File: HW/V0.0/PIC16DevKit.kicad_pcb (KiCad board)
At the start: 4 copper layers, 68.8 x 54 mm, 115 parts, among them J1 9V-12V, J2 USB C, J3 EXP PORT, J4 PG ICSP, Q1 SI2301, Q2 SI2302, Q3 SI2301, Q4 2N3906, Q5 SI2302, Q6 SI2302, Q7 SI2302, U1 LDO 3.3V/300mA, U10 20MHz, U11 PIC32MM0064GPM028, U2 MT1470, U3 MT3608, U4 PIC16F877A, U6 SN74LVC1T45, U7 SN74LVC1T45, U8 SN74LVC1T45, U9 SN74LVC1T45

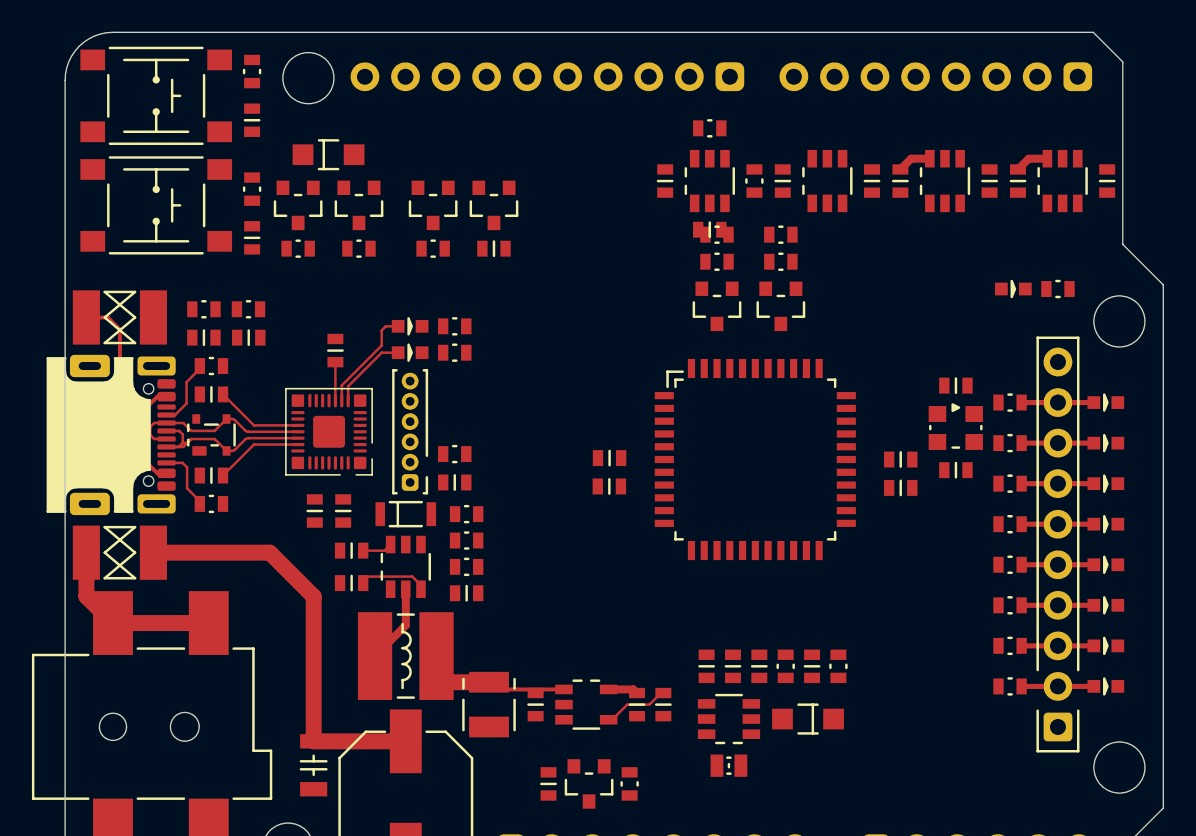
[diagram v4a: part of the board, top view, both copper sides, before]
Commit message: PIC16-DevKit-PCB-877 layout update 2
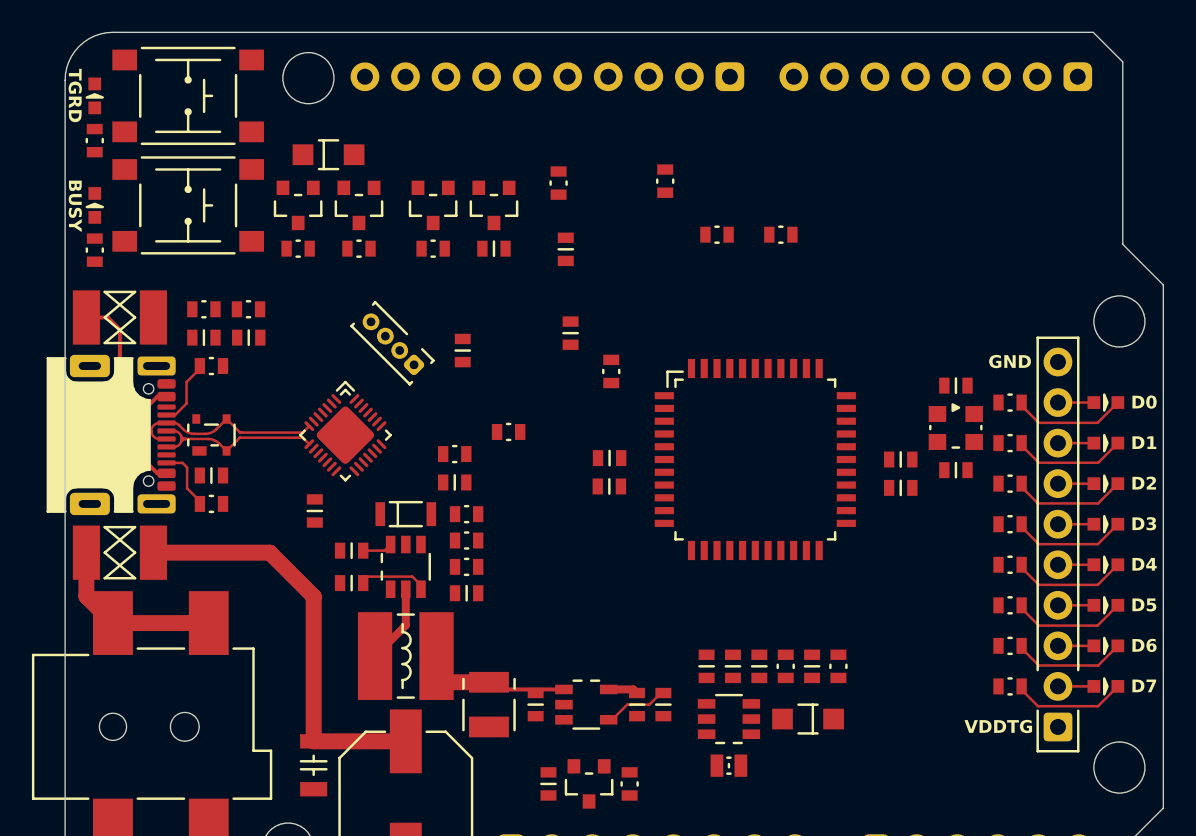
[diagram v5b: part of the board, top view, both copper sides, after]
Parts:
- removed C23, C24, C28, C30, C31, C33, C34, C35, C36: 100nF, SAMPI:CAP0603
- removed C29: 10uF, SAMPI:CAP0603
- removed D5: ULED, SAMPI:LED0603
- removed Q6, Q7: SI2302, SAMPI:SOT23
- removed R28, R30, R31: 5.1K, 1%, SAMPI:RES0603
- removed U11: PIC32MM0064GPM028, SAMPI:UQFN28-4x4-EP
- removed U6, U7, U8, U9: SN74LVC1T45, SAMPI:SOT-23-6_MCHP
- added U5: AVRxxDU28, SAMPI:VQFN28-4x4-EP, F.Cu at (78.2, 68.3)
- D10: value RD5 -> D2
- D11: value RD4 -> D3
- D12: value RD3 -> D4
- D13: value RD2 -> D5
- D14: value RD1 -> D6
- D15: value RD0 -> D7
- D6: value TARGET -> TGRD
- D8: value RD7 -> D0
- D9: value RD6 -> D1
- J4: value PG ICSP -> SIL04; footprint SAMPI:HD-1x6x1.27MM-TH -> SAMPI:HD-1x4x1.27MM-TH
- R19: value 330R -> 5.1K, 1%
- moved R19 35.6 mm to (88.5, 68.1)
- moved R24 26.2 mm to (62.5, 49.8), turned to 90 degrees
- moved D6 25.5 mm to (62.5, 47.0), turned to -90 degrees
- moved R23 25.2 mm to (94.9, 64.3)
- moved R25 23.0 mm to (62.5, 56.7), turned to 90 degrees
- moved C17 21.2 mm to (92.0, 56.6)
- moved D7 21.2 mm to (62.5, 53.9), turned to -90 degrees
- moved C22 20.8 mm to (92.3, 61.9)
- moved R18 20.4 mm to (91.6, 52.5)
- moved C25 7.98 mm to (85.6, 63.0)
- moved J4 5.65 mm to (81.2, 62.5), turned to 135 degrees
- moved R27 4.33 mm to (98.3, 52.4), turned to -90 degrees
- moved BT1 2.00 mm to (68.4, 53.9)
- moved BT2 2.00 mm to (68.4, 47.0)
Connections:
- net /PROGRAMMER/CS renamed /PROGRAMMER/TG_MCLR
- net /PROGRAMMER/~{PG_MCLR} renamed /PROGRAMMER/~{PG_RESET}
- C25 pad 1: +3.3V -> +5V
- C26 pad 1: +3.3V -> +5V
- C27 pad 1: +3.3V -> +5V
- D10 pad A: Net-(D10-PadA) -> /TARGET MCU/RD2
- D10 pad K: GND -> Net-(D10-PadK)
- D11 pad A: Net-(D11-PadA) -> /TARGET MCU/RD3
- D11 pad K: GND -> Net-(D11-PadK)
- D12 pad A: Net-(D12-PadA) -> /TARGET MCU/RD4
- D12 pad K: GND -> Net-(D12-PadK)
- D13 pad A: Net-(D13-PadA) -> /TARGET MCU/RD5
- D13 pad K: GND -> Net-(D13-PadK)
- D14 pad A: Net-(D14-PadA) -> /TARGET MCU/RD6
- D14 pad K: GND -> Net-(D14-PadK)
- D15 pad A: Net-(D15-PadA) -> /TARGET MCU/RD7
- D15 pad K: GND -> Net-(D15-PadK)
- D6 pad A: /PROGRAMMER/LED_TGRDY -> Net-(D6-PadA)
- D6 pad K: Net-(D6-PadK) -> GND
- D7 pad A: /PROGRAMMER/LED_BUSY -> Net-(D7-PadA)
- D7 pad K: Net-(D7-PadK) -> GND
- D8 pad A: Net-(D8-PadA) -> /TARGET MCU/RD0
- D8 pad K: GND -> Net-(D8-PadK)
- D9 pad A: Net-(D9-PadA) -> /TARGET MCU/RD1
- D9 pad K: GND -> Net-(D9-PadK)
- J3 pad 2: Net-(D15-PadA) -> /TARGET MCU/RD7
- J3 pad 3: Net-(D14-PadA) -> /TARGET MCU/RD6
- J3 pad 4: Net-(D13-PadA) -> /TARGET MCU/RD5
- J3 pad 5: Net-(D12-PadA) -> /TARGET MCU/RD4
- J3 pad 6: Net-(D11-PadA) -> /TARGET MCU/RD3
- J3 pad 7: Net-(D10-PadA) -> /TARGET MCU/RD2
- J3 pad 8: Net-(D9-PadA) -> /TARGET MCU/RD1
- J3 pad 9: Net-(D8-PadA) -> /TARGET MCU/RD0
- J4 pad 2: +3.3V -> +5V
- J4 pad 4: /PROGRAMMER/PG_PGD -> /PROGRAMMER/PG_UPDI
- MD1 pad 15: /PROGRAMMER/~{TG_RXD} -> /PROGRAMMER/TXD1
- MD1 pad 16: /PROGRAMMER/~{TG_TXD} -> /PROGRAMMER/RXD1
- MD1 pad 19: /TARGET MCU/ULED -> /TARGET MCU/GPIO
- MD1 pad 31: /PROGRAMMER/TG_SDA -> /PROGRAMMER/SDA
- MD1 pad 32: /PROGRAMMER/TG_SCL -> /PROGRAMMER/SCL
- R11 pad 1: /TARGET MCU/RD0 -> GND
- R11 pad 2: Net-(D15-PadA) -> Net-(D15-PadK)
- R12 pad 1: /TARGET MCU/RD1 -> GND
- R12 pad 2: Net-(D14-PadA) -> Net-(D14-PadK)
- R13 pad 1: /TARGET MCU/RD2 -> GND
- R13 pad 2: Net-(D13-PadA) -> Net-(D13-PadK)
- R14 pad 1: /TARGET MCU/RD3 -> GND
- R14 pad 2: Net-(D12-PadA) -> Net-(D12-PadK)
- R15 pad 1: /TARGET MCU/RD4 -> GND
- R15 pad 2: Net-(D11-PadA) -> Net-(D11-PadK)
- R16 pad 1: /TARGET MCU/RD5 -> GND
- R16 pad 2: Net-(D10-PadA) -> Net-(D10-PadK)
- R17 pad 1: /TARGET MCU/RD6 -> GND
- R17 pad 2: Net-(D9-PadA) -> Net-(D9-PadK)
- R19 pad 1: Net-(D5-PadK) -> +5V
- R19 pad 2: GND -> /PROGRAMMER/TG_PGD
- R20 pad 1: /TARGET MCU/RD7 -> GND
- R20 pad 2: Net-(D8-PadA) -> Net-(D8-PadK)
- R21 pad 2: /PROGRAMMER/TG_SCL -> /PROGRAMMER/SCL
- R22 pad 2: /PROGRAMMER/TG_SDA -> /PROGRAMMER/SDA
- R23 pad 1: +3.3V -> +5V
- R24 pad 1: Net-(D6-PadK) -> /PROGRAMMER/LED_TGRDY
- R24 pad 2: GND -> Net-(D6-PadA)
- R25 pad 1: Net-(D7-PadK) -> /PROGRAMMER/LED_BUSY
- R25 pad 2: GND -> Net-(D7-PadA)
- R26 pad 1: +3.3V -> +5V
- R27 pad 1: +VDDTG -> +5V
- R27 pad 2: /PROGRAMMER/~{TG_PGD} -> /PROGRAMMER/TG_PGC
- U4 pad 1: /PROGRAMMER/~{TG_RXD} -> /PROGRAMMER/TXD0
- U4 pad 11: /TARGET MCU/~{CS} -> /TARGET MCU/~{UBT}
- U4 pad 14: /TARGET MCU/SDI -> unconnected-(U4-RB4-Pad14)
- U4 pad 15: /TARGET MCU/SCLK -> unconnected-(U4-RB5-Pad15)
- U4 pad 16: /PROGRAMMER/~{TG_PGC} -> /PROGRAMMER/TG_PGC
- U4 pad 17: /PROGRAMMER/~{TG_PGD} -> /PROGRAMMER/TG_PGD
- U4 pad 26: /TARGET MCU/~{UBT} -> unconnected-(U4-RE1/~{WR}/AN6-Pad26)
- U4 pad 27: /TARGET MCU/ULED -> unconnected-(U4-RE2/~{CS}/AN7-Pad27)
- U4 pad 37: /PROGRAMMER/TG_SCL -> /PROGRAMMER/SCL
- U4 pad 42: /PROGRAMMER/TG_SDA -> /PROGRAMMER/SDA
- U4 pad 44: /PROGRAMMER/~{TG_TXD} -> /PROGRAMMER/RXD0
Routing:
- net +3.3V: track 9.78 -> 1.87 mm
- net Net-(D13-PadK): track 0.00 -> 7.19 mm
- net Net-(D8-PadK): track 0.00 -> 7.19 mm
- net Net-(D10-PadK): track 0.00 -> 7.18 mm
- net Net-(D15-PadK): track 0.00 -> 7.18 mm
- net Net-(D12-PadK): track 0.00 -> 7.18 mm
- net Net-(D11-PadK): track 0.00 -> 7.16 mm
- net Net-(D9-PadK): track 0.00 -> 7.13 mm
- net Net-(D14-PadK): track 0.00 -> 7.13 mm
- net /PROGRAMMER/LED_BUSY: track 6.57 -> 0.00 mm
- net Net-(U11-VCAP): track 5.49 -> 0.00 mm
- net /PROGRAMMER/LED_TGRDY: track 4.90 -> 0.00 mm
- net Net-(D12-PadA): track 4.53 -> 0.00 mm
- net Net-(D13-PadA): track 4.53 -> 0.00 mm
- net Net-(D11-PadA): track 4.53 -> 0.00 mm
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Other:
- board text added: "GND"
- board text added: "VDDTG"

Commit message: PIC16-DevKit-PCB-877 layout update 3: Add QWIIC port
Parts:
- added G***: LOGO, LOGO, F.Cu at (119.5, 52.0)
- added J5: QWIIC, SAMPI:HDM-1x4x1.0-RA, F.Cu at (124.6, 52.0)
- added Q6: SI2302, SAMPI:SOT23, F.Cu at (110.3, 52.0)
- added Q7: SI2302, SAMPI:SOT23, F.Cu at (114.9, 52.0)
- added R28: 5.1K, 1%, SAMPI:RES0603, F.Cu at (114.0, 57.0)
- added R30: 5.1K, 1%, SAMPI:RES0603, F.Cu at (118.2, 58.3)
- R4: value 100K -> 10K
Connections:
- R21 pad 2: /PROGRAMMER/SCL -> /PROGRAMMER/SDA
- R22 pad 2: /PROGRAMMER/SDA -> /PROGRAMMER/SCL
- U1 pad 3: +5V -> Net-(Q1-G)

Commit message: PIC16-DevKit-PCB-877 layout update 1
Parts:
- removed Q2: SI2302, SAMPI:SOT23
- moved C11 32.7 mm to (85.5, 56.0)
- moved C12 32.7 mm to (88.8, 56.0)
- moved C13 32.7 mm to (83.8, 56.0)
- moved C14 32.7 mm to (82.2, 56.0)
- moved L2 32.7 mm to (83.5, 62.2)
- moved R10 32.7 mm to (90.4, 56.0)
- moved R5 32.7 mm to (87.1, 56.0)
- moved D2 32.7 mm to (88.5, 59.3)
- moved U3 32.7 mm to (83.6, 59.3)
- moved R4 32.6 mm to (92.8, 87.9), turned to 0 degrees
- moved R29 31.6 mm to (69.8, 72.4), turned to 0 degrees
- moved Q1 31.6 mm to (92.8, 85.1)
- moved C9 29.5 mm to (95.3, 85.1), turned to 90 degrees
- moved Q5 26.6 mm to (71.2, 75.6), turned to 90 degrees
- moved C37 25.5 mm to (72.6, 72.4), turned to 0 degrees
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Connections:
- C7 pad 1: +5V -> +VDDTG
- Q1 pad 1: Net-(Q1-G) -> /POWER/~{VTG_EN}
- R19 pad 2: /PROGRAMMER/TG_PGD -> /PROGRAMMER/TG_PGC
- R27 pad 2: /PROGRAMMER/TG_PGC -> /PROGRAMMER/TG_PGD
- R4 pad 2: Net-(Q1-G) -> /POWER/~{VTG_EN}
- U1 pad 1: +5V -> +VDDTG
- U1 pad 3: Net-(Q1-G) -> +VDDTG
- U4 pad 14: unconnected-(U4-RB4-Pad14) -> /TARGET MCU/SDI
- U4 pad 15: unconnected-(U4-RB5-Pad15) -> /TARGET MCU/SCLK
- U4 pad 26: unconnected-(U4-RE1/~{WR}/AN6-Pad26) -> /TARGET MCU/~{CS}
- U4 pad 27: unconnected-(U4-RE2/~{CS}/AN7-Pad27) -> /TARGET MCU/GPIO
- U5 pad 13: unconnected-(U5-PD3/ACINN/AIN10-Pad13) -> /PROGRAMMER/TG_MCLR
- U5 pad 2: unconnected-(U5-PA4/MOSI/A2TX0/AIN2-Pad2) -> /PROGRAMMER/LED_TGRDY
- U5 pad 20: unconnected-(U5-PF0/AIN15/XTAL32K1-Pad20) -> /POWER/~{VTG_EN}
- U5 pad 21: unconnected-(U5-PF1/ANI16/XTAL32K2-Pad21) -> /POWER/VPP_EN
- U5 pad 26: unconnected-(U5-PA0/TX0/ASDA/XTALHF1-Pad26) -> /PROGRAMMER/TG_PGC
- U5 pad 27: unconnected-(U5-PA1/RX0/ASCL/XTALHF2-Pad27) -> /PROGRAMMER/TG_PGD
- U5 pad 3: unconnected-(U5-PA5/MISO/A2RX0/AIN3-Pad3) -> /PROGRAMMER/LED_BUSY
- U5 pad 5: unconnected-(U5-PA7/ACOUT/AIN5-Pad5) -> /PROGRAMMER/~{BT_MODE}
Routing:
- net +VDDTG: track 0.00 -> 198.7 mm, vias 0 -> 2
- net +5V: track 9.81 -> 136.0 mm, vias 0 -> 11
- net /PROGRAMMER/SDA: track 0.00 -> 86.9 mm, vias 0 -> 3
- net /PROGRAMMER/SCL: track 0.00 -> 77.6 mm, vias 0 -> 3
- net /PROGRAMMER/TXD1: track 0.00 -> 68.5 mm, vias 0 -> 1
- net /PROGRAMMER/RXD1: track 0.00 -> 67.6 mm, vias 0 -> 1
- net /TARGET MCU/~{UBT}: track 0.00 -> 67.4 mm, vias 0 -> 2
- net /PROGRAMMER/~{TG_MCLR}: track 0.00 -> 44.4 mm
- net /TARGET MCU/INT1: track 0.00 -> 39.6 mm, vias 0 -> 1
- net /TARGET MCU/AN5: track 0.00 -> 39.2 mm
- net /PROGRAMMER/TG_PGD: track 0.00 -> 37.9 mm, vias 0 -> 2
- net /PROGRAMMER/~{BT_MODE}: track 0.00 -> 36.7 mm
- net /PROGRAMMER/TG_PGC: track 0.00 -> 36.7 mm, vias 0 -> 2
- net /TARGET MCU/INT2: track 0.00 -> 34.3 mm, vias 0 -> 1
- net /TARGET MCU/INT0: track 0.00 -> 34.2 mm, vias 0 -> 1
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- added copper zone on B.Cu, net +5V
- added copper zone on F.Cu, net +5V
- added copper zone on In1.Cu, net +5V
- added copper zone on In2.Cu, net +5V
- added copper zone on F.Cu, net Net-(F1-Pad1)
- added copper zone on F.Cu, net Net-(F2-Pad1)
- added copper zone on F.Cu, net VDC
- added copper zone on In2.Cu, net VDC
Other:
- board text added: "+3V3"
- board text added: "+5V0"
- board text added: "+VDC"
- board text added: "AN0"
- board text added: "AN1"
- board text added: "AN2"
- board text added: "AN3"
- board text added: "AN4"
- board text added: "AN5"
- board text added: "INT0"
- board text added: "INT1"
- board text added: "INT2"
- board text added: "NC"
- board text added: "PWM1"
- board text added: "PWM2"
- board text added: "RXD1"
- board text added: "SCL"
- board text added: "SD0"
- board text added: "SDA"
- board text added: "T0CKI"
- board text added: "T1CKI"
- board text added: "TXD1"
- board text added: "~{MCLR}"
